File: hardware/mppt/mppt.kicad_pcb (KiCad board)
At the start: 4 copper layers, 160 x 160 mm, 355 parts, among them IC1301 INA229AIDGSR, IC1501 LMR38010SDDAR, IC1502 TPS2121, IC801 INA229AIDGSR, IC901 SN74LVC08APWR, IC902 SN74LVC1G04DBVR, IC903 SN74HCS367PWR, IC904 SN74LVC2G32DCUR, J1401 Conn_01x04, J1402 Conn_01x02, J1403 Conn_02x04_Odd_Even, J1404 Conn_01x10, J1405 USB_C_Plug_USB2.0, J1501 Conn_01x02, J1502 CT3151, J1503 CT3151, J1504 CT3151, J301 Conn_01x01, J302 Conn_01x01, J303 CT3151, J304 CT3151, J305 CT3151, J306 CT3151, J307 Conn_01x01, J308 Conn_01x01, J401 Conn_01x02, J402 Conn_01x03, J403 Conn_01x03, J404 Conn_01x03, Q1001 Q_NMOS_GDS, Q1101 Q_NMOS_SGD, Q1102 Q_NMOS_SGD, Q1201 Q_NMOS_SGD, Q1202 Q_NMOS_SGD, Q401 Q_NMOS_GDS, Q501 EPC2059, Q502 EPC2059, Q601 Q_NMOS_GDS, Q701 Q_NMOS_GDS, SW201 SW_SPST, U1001 ADUM4221-1ARIZ, U1101 TPSI3050, U1201 TPSI3050, U1401 ISO1044BD, U1402 USBLC6-2SC6, U1501 AP63205WU, U1502 TLV75733PDBV, U201 STM32F446RETx, U401 MCP9700Ax-ELT, Y201 16MHz, Y202 32kHz

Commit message: PCB variant for power regulation breakout.
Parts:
- removed C1001, C1003, C1004, C204: 10u, Capacitor_SMD:C_1206_3216Metric_Pad1.33x1.80mm_HandSolder
- removed C1002, C1005, C1006, C1102, C1202, C1301, C1302, C1401, C1402, C203, C205, C208, C209, C211, C212, C213, C801, C802, C901, C902, C903, C904: 100n, Capacitor_SMD:C_0402_1005Metric_Pad0.74x0.62mm_HandSolder
- removed C1101, C1103, C1104, C1201, C1203, C1204, C214, C401, C402: 1u, Capacitor_SMD:C_0603_1608Metric_Pad1.08x0.95mm_HandSolder
- removed C1516, C1517: 22u, Capacitor_SMD:C_1210_3225Metric_Pad1.33x2.70mm_HandSolder
- removed C201, C206: 10p, Capacitor_SMD:C_0402_1005Metric_Pad0.74x0.62mm_HandSolder
- removed C202, C207: 15p, Capacitor_SMD:C_0402_1005Metric_Pad0.74x0.62mm_HandSolder
- removed C210: 4.7u, Capacitor_SMD:C_0805_2012Metric_Pad1.18x1.45mm_HandSolder
- removed C501, C505: 100n, Capacitor_SMD:C_1206_3216Metric_Pad1.33x1.80mm_HandSolder
- removed C502, C506: 1u, Capacitor_SMD:C_2220_5750Metric_Pad1.97x5.40mm_HandSolder
- removed C503, C507: 2.2u, Capacitor_SMD:C_2220_5750Metric_Pad1.97x5.40mm_HandSolder
- removed C504, C508, C509: 18u, Capacitor_THT:C_Radial_D10.0mm_H16.0mm_P5.00mm
- removed D1001, D1003, D1004, D1101, D1201, D401, D601, D701: Schottky, Diode_SMD:D_SOD-123F
- removed D1002, D1005: Zener, Diode_SMD:D_SOD-123F
- removed D1507, D201, D202, D203: RED, LED_SMD:LED_0805_2012Metric_Pad1.15x1.40mm_HandSolder
- removed D501, D503: 150, Diode_SMD:D_SMA_Handsoldering
- removed D502: SMAJ150CA, Diode_SMD:D_SMA_Handsoldering
- removed D602, D702: BLU, LED_SMD:LED_0805_2012Metric_Pad1.15x1.40mm_HandSolder
- removed F501, F502: Fuse, footprints:littelfuse_65600001009
- removed FB201: FerriteBead, Resistor_SMD:R_0603_1608Metric_Pad0.98x0.95mm_HandSolder
- removed H401, H402, H403, H404: MountingHole, MountingHole:MountingHole_2.7mm_M2.5
- removed IC1301, IC801: INA229AIDGSR, footprints:ti_INA229_AIDGSR
- removed IC901: SN74LVC08APWR, footprints:ti_SN74LVC08A_PWR
- removed IC902: SN74LVC1G04DBVR, footprints:ti_SN74LVC1G04_DBVR
- removed IC903: SN74HCS367PWR, footprints:ti_SN74HCS367_PWR
- removed IC904: SN74LVC2G32DCUR, footprints:ti_SN74LVC2G32_DCUR
- removed J1401: Conn_01x04, Connector_Molex:Molex_Micro-Fit_3.0_43650-0415_1x04_P3.00mm_Vertical
- removed J1402: Conn_01x02, Connector_PinHeader_2.54mm:PinHeader_1x02_P2.54mm_Vertical
- removed J1403: Conn_02x04_Odd_Even, Connector_PinHeader_2.54mm:PinHeader_2x04_P2.54mm_Vertical
- removed J1404: Conn_01x10, Connector_PinSocket_2.54mm:PinSocket_1x10_P2.54mm_Vertical
- removed J1405: USB_C_Plug_USB2.0, Connector_USB:USB_C_Receptacle_GCT_USB4105-xx-A_16P_TopMnt_Horizontal
- removed J301, J302, J307, J308: Conn_01x01, footprints:ke_7771_SEMS
- removed J303, J304, J305, J306: CT3151, footprints:caltest_ct3151
- removed J401: Conn_01x02, Connector_Molex:Molex_Micro-Fit_3.0_43650-0215_1x02_P3.00mm_Vertical
- removed J402, J403, J404: Conn_01x03, Connector_Molex:Molex_Micro-Fit_3.0_43650-0315_1x03_P3.00mm_Vertical
- removed JP201: Jumper_3_Bridged12, Connector_PinSocket_2.54mm:PinSocket_1x03_P2.54mm_Vertical
- removed L1503: 10u, Inductor_SMD:L_Bourns_SRN6045TA
- removed L501: 471u, footprints:ferroxcube_PQ32_30_3C97_wire
- removed LB501: CPV-PQ32/30-1S-12P-Z, footprints:ferroxcube_CPV-PQ32_30-1S-12P-Z
- removed NT1001, NT1301, NT601, NT701, NT801: NetTie_2, NetTie:NetTie-2_SMD_Pad0.5mm
- removed NT501: NetTie_3_Tee, NetTie:NetTie-3_SMD_Pad2.0mm
- removed PS1501: CRE1S0505MEC, footprints:murata_CRE1_S0505MEC
- removed Q1001, Q401, Q601, Q701: Q_NMOS_GDS, Package_TO_SOT_SMD:SOT-223-3_TabPin2
- removed Q1101, Q1102, Q1201, Q1202: Q_NMOS_SGD, Package_SO:PowerPAK_SO-8_Single
- removed Q501, Q502: EPC2059, footprints:epc_EPC2059
- removed R1001, R204, R901, R902, R903, R904, R905, R906, R907: 10k, Resistor_SMD:R_0603_1608Metric_Pad0.98x0.95mm_HandSolder
- removed R1002, R1003, R1004, R1005, R203: 0, Resistor_SMD:R_1210_3225Metric_Pad1.30x2.65mm_HandSolder
- removed R1006: 1.5, Resistor_SMD:R_1210_3225Metric_Pad1.30x2.65mm_HandSolder
- removed R1101, R1201: 7.32k, Resistor_SMD:R_0603_1608Metric_Pad0.98x0.95mm_HandSolder
- removed R1102, R1103, R1202, R1203, R601, R602, R701, R702: 15, Resistor_SMD:R_1210_3225Metric_Pad1.30x2.65mm_HandSolder
- removed R1301, R801: 86.6k, Resistor_SMD:R_0603_1608Metric_Pad0.98x0.95mm_HandSolder
- removed R1302, R1402, R1403, R1404, R802: 100k, Resistor_SMD:R_0603_1608Metric_Pad0.98x0.95mm_HandSolder
- removed R1303, R1305, R803, R805: 15, Resistor_SMD:R_0603_1608Metric_Pad0.98x0.95mm_HandSolder
- removed R1304, R804: 4m, Resistor_SMD:R_Shunt_Vishay_WSKW0612
- removed R1401: 120, Resistor_SMD:R_0603_1608Metric_Pad0.98x0.95mm_HandSolder
- removed R1405, R1406: 5.1k, Resistor_SMD:R_0603_1608Metric_Pad0.98x0.95mm_HandSolder
- removed R1520, R201, R202, R205, R401, R402: 3.3k, Resistor_SMD:R_0603_1608Metric_Pad0.98x0.95mm_HandSolder
- removed R403: 205, Resistor_SMD:R_0603_1608Metric_Pad0.98x0.95mm_HandSolder
- removed R603, R703: 10k, Resistor_SMD:R_2512_6332Metric_Pad1.40x3.35mm_HandSolder
- removed the REF** at (138.0, 195.1)
- removed SW201: SW_SPST, Button_Switch_THT:SW_PUSH_6mm
- removed TP1001, TP1002, TP1003, TP1004, TP1005, TP1006, TP1007, TP1101, TP1102, TP1103, TP1104, TP1105, TP1201, TP1202, TP1203, TP1204, TP1205, TP1301, TP1302, TP1303, TP1304, TP1305, TP1306, TP1307, TP1405, TP1406, TP1407, TP1408, TP1409, TP1410, TP1411, TP1412, TP1413, TP1414, TP1415, TP1416, TP1417, TP1418, TP1419, TP1420, TP1421, TP203, TP204, TP205, TP206, TP207, TP208, TP209, TP210, TP404, TP405, TP406, TP407, TP408, TP409, TP601, TP602, TP603, TP604, TP701, TP702, TP703, TP704, TP802, TP803, TP804, TP805, TP806, TP807, TP808, TP901, TP902, TP903, TP904, TP905, TP906: TestPoint_Small, TestPoint:TestPoint_Pad_D1.0mm
- removed TP1308, TP1309, TP503, TP504, TP809, TP810: TestPoint_2Pole, TestPoint:TestPoint_2Pads_Pitch2.54mm_Drill0.8mm
- removed TP1401, TP1402, TP1403, TP1404, TP201, TP202, TP301, TP302, TP303, TP401, TP402, TP403, TP501, TP502, TP505, TP506, TP507: TestPoint, TestPoint:TestPoint_Keystone_5000-5004_Miniature
- removed U1001: ADUM4221-1ARIZ, footprints:ad_ADUM4221_1ARIZ
- removed U1101, U1201: TPSI3050, footprints:ti_TPS3050_DWZ
- removed U1401: ISO1044BD, Package_SO:SOIC-8_3.9x4.9mm_P1.27mm
- removed U1402: USBLC6-2SC6, Package_TO_SOT_SMD:SOT-23-6
- removed U201: STM32F446RETx, Package_QFP:LQFP-64_10x10mm_P0.5mm
- removed U401: MCP9700Ax-ELT, Package_TO_SOT_SMD:SOT-353_SC-70-5
- removed VR1001: PV36W104C01B00, footprints:bourns_PV36W201C01B00
- removed Y201: 16MHz, Crystal:Crystal_SMD_Abracon_ABM8G-4Pin_3.2x2.5mm
- removed Y202: 32kHz, Crystal:Crystal_SMD_Abracon_ABS25-4Pin_8.0x3.8mm
- C1501, C1503, C1507, NT1501, REF** (x2): moved to B.Cu
- C1502, C1505, C1506, C1509, C1510, IC1501, L1501, L1502, R1502, R1513, R1514, R1516, U1501, U1502: moved to F.Cu
- C1511: value 22u -> 1u; footprint Capacitor_SMD:C_1210_3225Metric_Pad1.33x2.70mm_HandSolder -> Capacitor_SMD:C_0603_1608Metric_Pad1.08x0.95mm_HandSolder
- C1512: value 1u -> 10u; footprint Capacitor_SMD:C_0603_1608Metric_Pad1.08x0.95mm_HandSolder -> Capacitor_SMD:C_1206_3216Metric_Pad1.33x1.80mm_HandSolder; moved to B.Cu
- C1513: value 10u -> 100n; footprint Capacitor_SMD:C_1206_3216Metric_Pad1.33x1.80mm_HandSolder -> Capacitor_SMD:C_0402_1005Metric_Pad0.74x0.62mm_HandSolder; moved to B.Cu
- C1514: value 100n -> 22u; footprint Capacitor_SMD:C_0402_1005Metric_Pad0.74x0.62mm_HandSolder -> Capacitor_SMD:C_1210_3225Metric_Pad1.33x2.70mm_HandSolder
- C1515: value 4.7u -> 22u; footprint Capacitor_SMD:C_0805_2012Metric_Pad1.18x1.45mm_HandSolder -> Capacitor_SMD:C_1210_3225Metric_Pad1.33x2.70mm_HandSolder
- D1501: footprint Diode_SMD:D_SMA_Handsoldering -> Diode_SMD:D_SMA
- D1502: footprint Diode_SMD:D_SMA_Handsoldering -> Diode_SMD:D_SMA; moved to B.Cu
- H101, H102, H103, H104: footprint MountingHole:MountingHole_3.2mm_M3 -> MountingHole:MountingHole_2.7mm_M2.5_DIN965_Pad_TopBottom
- REF**: value Symbol_HighVoltage_Triangle_6x6mm_Copper -> Symbol_HighVoltage_NoTriangle_2x5mm_Copper; footprint Symbol:Symbol_HighVoltage_Triangle_6x6mm_Copper -> Symbol:Symbol_HighVoltage_NoTriangle_2x5mm_Copper
- moved J1504 285.0 mm to (54.0, 82.8), turned to 0 degrees
- moved TP1508 269.3 mm to (48.5, 55.0)
- moved J1503 266.0 mm to (70.0, 82.8), turned to 0 degrees
- moved TP1507 264.6 mm to (48.5, 63.0), turned to 90 degrees
- moved TP1506 259.3 mm to (48.5, 71.0)
- moved J1502 251.3 mm to (86.0, 82.8), turned to 0 degrees
- moved TP1504 246.1 mm to (64.0, 57.7)
- moved TP1505 243.6 mm to (64.2, 69.2)
- moved C1511 242.8 mm to (57.0, 58.4), turned to 0 degrees
- moved D1505 234.4 mm to (48.5, 59.0)
- moved R1518 234.4 mm to (48.5, 59.0)
- moved C1515 232.1 mm to (57.5, 65.1), turned to 0 degrees
- moved D1506 226.5 mm to (48.5, 67.0), turned to 90 degrees
- moved R1519 226.5 mm to (48.5, 67.0), turned to 90 degrees
- moved TP1503 225.0 mm to (79.2, 71.4)
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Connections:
- C1512 pad 1: +5V -> +3V3
- C1513 pad 1: +3V3 -> Net-(U1501-BST)
- C1513 pad 2: GND -> Net-(U1501-SW)
- C1514 pad 1: Net-(U1501-BST) -> +5V
- C1514 pad 2: Net-(U1501-SW) -> GND
- C1515 pad 1: +5VL -> +5V
- C1515 pad 2: GND1 -> GND
- IC1501 pad 5: /power regulation/BUCK_PG -> /power regulation/BUCK_FB
- IC1501 pad 6: /power regulation/BUCK_FB -> /power regulation/BUCK_PG
- R1513 pad 2: /power regulation/BUCK_FB -> /power regulation/BUCK_PG
- R1515 pad 2: /power regulation/BUCK_PG -> /power regulation/BUCK_FB
- R1516 pad 1: /power regulation/BUCK_PG -> /power regulation/BUCK_FB
- TP1506 pad 1: +5V -> +12V
- TP1507 pad 1: +5VL -> +5V
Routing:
- net +12V: track 0.00 -> 37.2 mm, vias 0 -> 8
- net +12C: track 0.00 -> 32.1 mm, vias 0 -> 8
- net Net-(JP1501-A): track 0.00 -> 20.3 mm, vias 0 -> 1
- net GND: track 0.00 -> 20.2 mm, vias 0 -> 22
- net /VI-: track 0.00 -> 17.5 mm, vias 0 -> 12
- net +5V: track 0.00 -> 15.1 mm, vias 0 -> 1
- net /VI+: track 1.84 -> 14.0 mm, vias 0 -> 12
- net /power regulation/OV2: track 0.00 -> 8.85 mm, vias 0 -> 1
- net /power regulation/OV1: track 0.00 -> 8.85 mm, vias 0 -> 1
- net /power regulation/PR1: track 0.00 -> 8.07 mm, vias 0 -> 1
- net /power regulation/CP2: track 0.00 -> 7.93 mm, vias 0 -> 1
- net +12L: track 0.00 -> 5.62 mm, vias 0 -> 6
- net +3V3: track 0.00 -> 5.55 mm, vias 0 -> 1
- net /power regulation/BUCK_FB: track 1.85 -> 5.15 mm, vias 0 -> 1
- net Net-(IC1501-EN): track 8.54 -> 5.44 mm, vias 0 -> 1
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- added copper zone on F.Cu, net +12C
- added copper zone on F.Cu, net +12L
- added copper zone on F.Cu, net +12V
- added copper zone on F.Cu, net +3V3
- added copper zone on F.Cu, net +5V
- added copper zone on F.Cu, net /VI+
- added copper zone on B.Cu, net /VI-
- added copper zone on F.Cu, net /VI-
- added copper zone on In1.Cu, net /VI-
- added copper zone on In2.Cu, net /VI-
- added copper zone on B.Cu, net GND
- added copper zone on In1.Cu, net GND
- added copper zone on In2.Cu, net GND
- added copper zone on F.Cu, net Net-(IC1501-SW)
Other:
- board size 160 x 160 mm -> 50 x 50 mm
- board text added: "12C"
- board text added: "12L"
- board text added: "12V"
- board text added: "3V3"
- board text added: "5V"
- board text added: "CARPWR"
- board text added: "GND"
- board text added: "Mighty MPPT Power Regulation Breakout v0.1.0rc Matthew Yu & Jacob Pustilnik"
- board text added: "VI+"
- board text added: "VI-"
- board text removed: "80-150V"
- board text removed: "BANANA FOR SCALE"
- board text removed: "Mighty MPPT Power Converter Breakout v0.1.0rc Matthew Yu & Jacob Pustilnik"

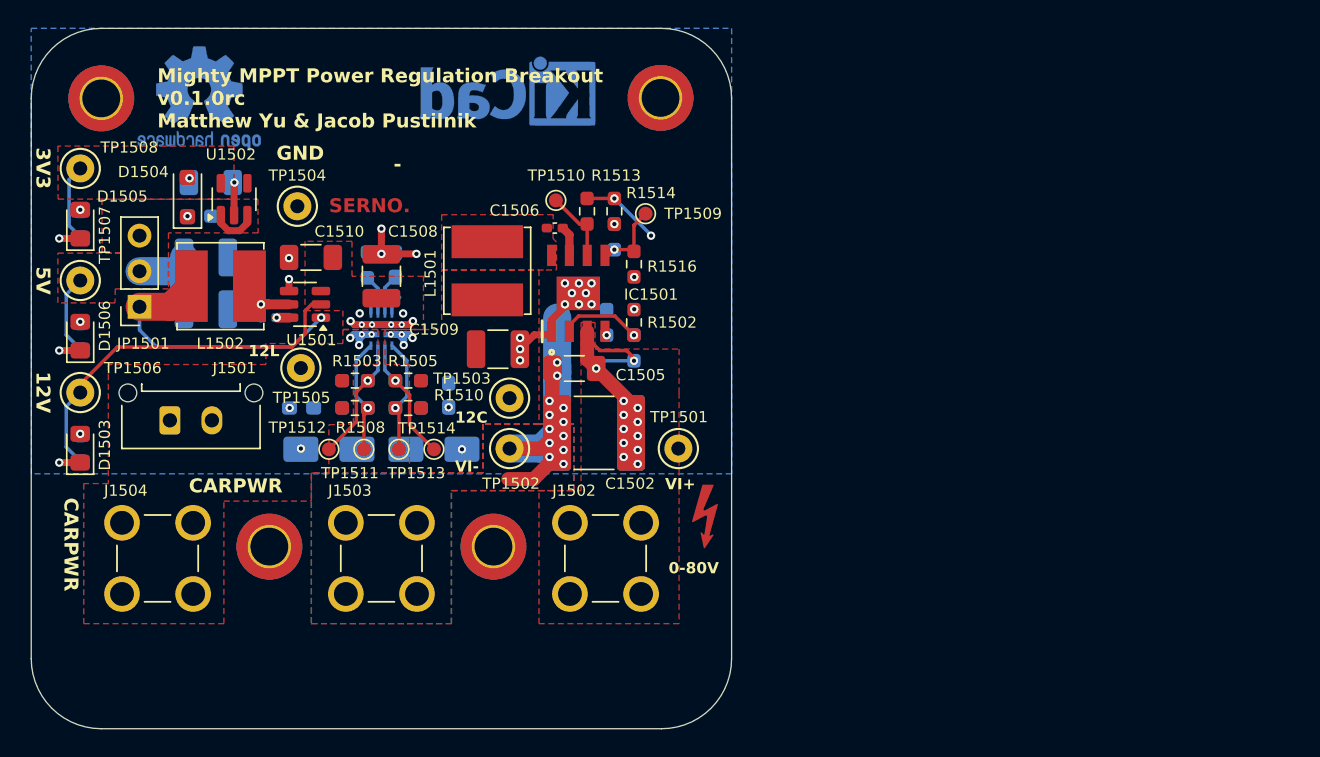
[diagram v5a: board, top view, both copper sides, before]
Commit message: complete layout, drc, signaling optimizations and added dnp testpoints
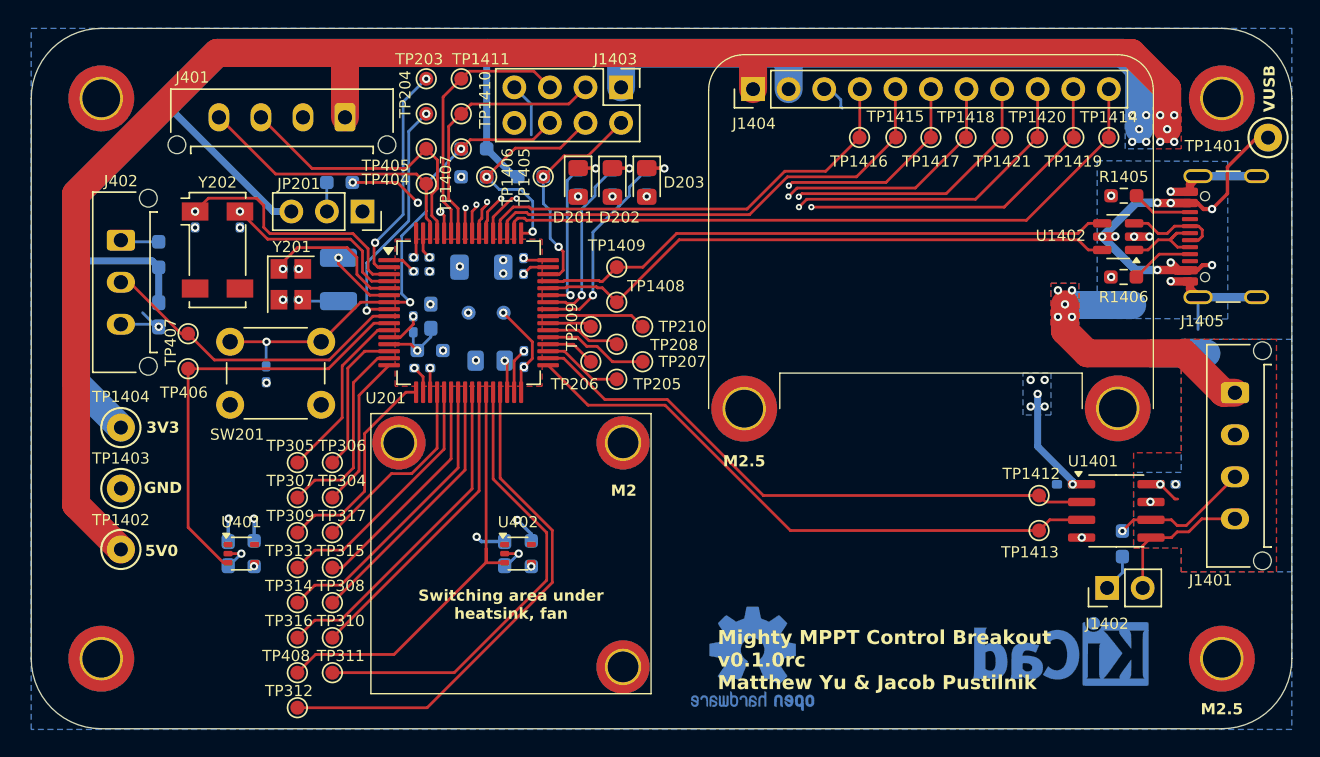
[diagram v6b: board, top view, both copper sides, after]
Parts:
- removed C1501, C1504, C1507, C1511: 1u, Capacitor_SMD:C_0603_1608Metric_Pad1.08x0.95mm_HandSolder
- removed C1502, C1503: 2.2u, Capacitor_SMD:C_2220_5750Metric_Pad1.97x5.40mm_HandSolder
- removed C1505: 100n, Capacitor_SMD:C_1206_3216Metric_Pad1.33x1.80mm_HandSolder
- removed C1506, C1513: 100n, Capacitor_SMD:C_0402_1005Metric_Pad0.74x0.62mm_HandSolder
- removed C1508, C1509, C1514, C1515: 22u, Capacitor_SMD:C_1210_3225Metric_Pad1.33x2.70mm_HandSolder
- removed C1510, C1512: 10u, Capacitor_SMD:C_1206_3216Metric_Pad1.33x1.80mm_HandSolder
- removed D1501, D1502: SMAJ15CA, Diode_SMD:D_SMA
- removed D1503, D1505, D1506: RED, LED_SMD:LED_0805_2012Metric_Pad1.15x1.40mm_HandSolder
- removed D1504: Schottky, Diode_SMD:D_SOD-123F
- removed IC1501: LMR38010SDDAR, footprints:ti_LMR38010_SDDAR
- removed IC1502: TPS2121, footprints:ti_TPS2121_RUXR
- removed J1501: Conn_01x02, Connector_Molex:Molex_Micro-Fit_3.0_43650-0215_1x02_P3.00mm_Vertical
- removed J1502, J1503, J1504: CT3151, footprints:caltest_ct3151
- removed JP1501: Jumper_3_Bridged12, Connector_PinSocket_2.54mm:PinSocket_1x03_P2.54mm_Vertical
- removed L1501: 68u, Inductor_SMD:L_Bourns_SRN6045TA
- removed L1502: 4.7u, Inductor_SMD:L_Bourns_SRN6045TA
- removed NT1501: NetTie_2, NetTie:NetTie-2_SMD_Pad2.0mm
- removed R1501, R1503, R1505, R1508, R1510, R1513, R1514: 100k, Resistor_SMD:R_0603_1608Metric_Pad0.98x0.95mm_HandSolder
- removed R1502, R1515, R1516, R1517: 10k, Resistor_SMD:R_0603_1608Metric_Pad0.98x0.95mm_HandSolder
- removed R1504, R1506: 7.68k, Resistor_SMD:R_0603_1608Metric_Pad0.98x0.95mm_HandSolder
- removed R1507, R1512: 64.9k, Resistor_SMD:R_0603_1608Metric_Pad0.98x0.95mm_HandSolder
- removed R1509: 17.4k, Resistor_SMD:R_0603_1608Metric_Pad0.98x0.95mm_HandSolder
- removed R1511: 14k, Resistor_SMD:R_0603_1608Metric_Pad0.98x0.95mm_HandSolder
- removed R1518, R1519: 3.3k, Resistor_SMD:R_0603_1608Metric_Pad0.98x0.95mm_HandSolder
- removed the REF** at (93.3, 80.0)
- removed TP1501, TP1502, TP1503, TP1504, TP1505, TP1506, TP1507, TP1508: TestPoint, TestPoint:TestPoint_Keystone_5000-5004_Miniature
- removed TP1509, TP1510, TP1511, TP1512, TP1513, TP1514: TestPoint_Small, TestPoint:TestPoint_Pad_D1.0mm
- removed U1501: AP63205WU, Package_TO_SOT_SMD:TSOT-23-6
- removed U1502: TLV75733PDBV, Package_TO_SOT_SMD:SOT-23-5
- added C1401: 100n, Capacitor_SMD:C_0402_1005Metric_Pad0.74x0.62mm_HandSolder, B.Cu at (118.8, 77.5)
- added C1402: 100n, Capacitor_SMD:C_0402_1005Metric_Pad0.74x0.62mm_HandSolder, B.Cu at (126.1, 77.5)
- added C201: 10p, Capacitor_SMD:C_0402_1005Metric_Pad0.74x0.62mm_HandSolder, B.Cu at (63.5, 62.2)
- added C202: 15p, Capacitor_SMD:C_0402_1005Metric_Pad0.74x0.62mm_HandSolder, B.Cu at (56.7, 58.6)
- added C203: 100n, Capacitor_SMD:C_0402_1005Metric_Pad0.74x0.62mm_HandSolder, B.Cu at (61.8, 69.7)
- added C204: 10u, Capacitor_SMD:C_1206_3216Metric_Pad1.33x1.80mm_HandSolder, B.Cu at (77.1, 62.0)
- added C205: 100n, Capacitor_SMD:C_0402_1005Metric_Pad0.74x0.62mm_HandSolder, B.Cu at (72.9, 61.4)
- added C206: 10p, Capacitor_SMD:C_0402_1005Metric_Pad0.74x0.62mm_HandSolder, B.Cu at (63.5, 64.4)
- added C207: 15p, Capacitor_SMD:C_0402_1005Metric_Pad0.74x0.62mm_HandSolder, B.Cu at (59.9, 58.6)
- added C208: 100n, Capacitor_SMD:C_0402_1005Metric_Pad0.74x0.62mm_HandSolder, B.Cu at (80.2, 62.0)
- added C209: 100n, Capacitor_SMD:C_0402_1005Metric_Pad0.74x0.62mm_HandSolder, B.Cu at (72.9, 62.4)
- added C210: 4.7u, Capacitor_SMD:C_0805_2012Metric_Pad1.18x1.45mm_HandSolder, B.Cu at (77.8, 68.7)
- added C211: 100n, Capacitor_SMD:C_0402_1005Metric_Pad0.74x0.62mm_HandSolder, B.Cu at (80.2, 68.6)
- added C212: 100n, Capacitor_SMD:C_0402_1005Metric_Pad0.74x0.62mm_HandSolder, B.Cu at (72.9, 69.2)
- added C213: 100n, Capacitor_SMD:C_0402_1005Metric_Pad0.74x0.62mm_HandSolder, B.Cu at (72.3, 66.1)
- added C214: 1u, Capacitor_SMD:C_0603_1608Metric_Pad1.08x0.95mm_HandSolder, B.Cu at (73.5, 65.5)
- added C401: 1u, Capacitor_SMD:C_0603_1608Metric_Pad1.08x0.95mm_HandSolder, B.Cu at (59.1, 82.5)
- added C402: 1u, Capacitor_SMD:C_0603_1608Metric_Pad1.08x0.95mm_HandSolder, B.Cu at (78.8, 82.5)
- added C403: 1u, Capacitor_SMD:C_0603_1608Metric_Pad1.08x0.95mm_HandSolder, B.Cu at (54.1, 65.5)
- added D201: RED, LED_SMD:LED_0805_2012Metric_Pad1.15x1.40mm_HandSolder, F.Cu at (84.0, 56.0)
- added D202: RED, LED_SMD:LED_0805_2012Metric_Pad1.15x1.40mm_HandSolder, F.Cu at (86.5, 56.0)
- added D203: RED, LED_SMD:LED_0805_2012Metric_Pad1.15x1.40mm_HandSolder, F.Cu at (88.9, 56.0)
- added FB201: FerriteBead, Resistor_SMD:R_0603_1608Metric_Pad0.98x0.95mm_HandSolder, B.Cu at (73.5, 68.0)
- added H1401: MountingHole, MountingHole:MountingHole_2.7mm_M2.5_DIN965_Pad_TopBottom, F.Cu at (95.9, 72.2)
- added H1402: MountingHole, MountingHole:MountingHole_2.7mm_M2.5_DIN965_Pad_TopBottom, F.Cu at (122.6, 72.1)
- added H401: MountingHole, MountingHole:MountingHole_2.2mm_M2_DIN965_Pad_TopBottom, F.Cu at (87.2, 74.6)
- added H402: MountingHole, MountingHole:MountingHole_2.2mm_M2_DIN965_Pad_TopBottom, F.Cu at (71.2, 74.6)
- added H403: MountingHole, MountingHole:MountingHole_2.2mm_M2_DIN965_Pad_TopBottom, F.Cu at (87.2, 90.6)
- added J1401: Conn_01x04, Connector_Molex:Molex_Micro-Fit_3.0_43650-0415_1x04_P3.00mm_Vertical, F.Cu at (130.9, 71.0)
- added J1402: Conn_01x02, Connector_PinHeader_2.54mm:PinHeader_1x02_P2.54mm_Vertical, F.Cu at (121.8, 85.0)
- added J1403: Conn_02x04_Odd_Even, Connector_PinHeader_2.54mm:PinHeader_2x04_P2.54mm_Vertical, F.Cu at (87.1, 49.2)
- added J1404: Conn_01x11, Connector_PinHeader_2.54mm:PinHeader_1x11_P2.54mm_Vertical, F.Cu at (96.5, 49.3)
- added J1405: USB_C_Plug_USB2.0, Connector_USB:USB_C_Receptacle_GCT_USB4105-xx-A_16P_TopMnt_Horizontal, F.Cu at (131.4, 59.9)
- added J401: Conn_01x04, Connector_Molex:Molex_Micro-Fit_3.0_43650-0415_1x04_P3.00mm_Vertical, F.Cu at (67.4, 51.4)
- added J402: Conn_01x03, Connector_Molex:Molex_Micro-Fit_3.0_43650-0315_1x03_P3.00mm_Vertical, F.Cu at (51.4, 60.1)
- added JP201: Jumper_3_Bridged12, Connector_PinSocket_2.54mm:PinSocket_1x03_P2.54mm_Vertical, F.Cu at (68.7, 58.1)
- added NT1401: NetTie_2, NetTie:NetTie-2_SMD_Pad2.0mm, B.Cu at (126.9, 68.2)
- added NT1402: NetTie_2, NetTie:NetTie-2_SMD_Pad2.0mm, B.Cu at (121.6, 64.8)
- added R1401: 120, Resistor_SMD:R_0603_1608Metric_Pad0.98x0.95mm_HandSolder, B.Cu at (122.9, 81.8)
- added R1402: 100k, Resistor_SMD:R_0603_1608Metric_Pad0.98x0.95mm_HandSolder, B.Cu at (76.6, 53.6)
- added R1403: 100k, Resistor_SMD:R_0603_1608Metric_Pad0.98x0.95mm_HandSolder, B.Cu at (80.7, 55.6)
- added R1404: 100k, Resistor_SMD:R_0603_1608Metric_Pad0.98x0.95mm_HandSolder, B.Cu at (76.6, 55.6)
- added R1405: 5.1k, Resistor_SMD:R_0603_1608Metric_Pad0.98x0.95mm_HandSolder, F.Cu at (123.0, 57.0)
- added R1406: 5.1k, Resistor_SMD:R_0603_1608Metric_Pad0.98x0.95mm_HandSolder, F.Cu at (123.0, 62.8)
- added R201: 3.3k, Resistor_SMD:R_0603_1608Metric_Pad0.98x0.95mm_HandSolder, B.Cu at (84.0, 56.0)
- added R202: 3.3k, Resistor_SMD:R_0603_1608Metric_Pad0.98x0.95mm_HandSolder, B.Cu at (86.5, 56.0)
- added R203: 0, Resistor_SMD:R_1210_3225Metric_Pad1.30x2.65mm_HandSolder, B.Cu at (66.9, 62.9)
- added R204: 100k, Resistor_SMD:R_0603_1608Metric_Pad0.98x0.95mm_HandSolder, B.Cu at (67.0, 56.0)
- added R205: 3.3k, Resistor_SMD:R_0603_1608Metric_Pad0.98x0.95mm_HandSolder, B.Cu at (88.9, 56.0)
- added R401: 205, Resistor_SMD:R_0603_1608Metric_Pad0.98x0.95mm_HandSolder, B.Cu at (60.9, 82.5)
- added R402: 205, Resistor_SMD:R_0603_1608Metric_Pad0.98x0.95mm_HandSolder, B.Cu at (80.7, 82.5)
- added R403: 205, Resistor_SMD:R_0603_1608Metric_Pad0.98x0.95mm_HandSolder, B.Cu at (54.1, 61.1)
- added SW201: SW_SPST, Button_Switch_THT:SW_PUSH_6mm, F.Cu at (65.7, 71.9)
- added TP1401: TestPoint, TestPoint:TestPoint_Keystone_5000-5004_Miniature, F.Cu at (133.3, 52.8)
- added TP1402: TestPoint, TestPoint:TestPoint_Keystone_5000-5004_Miniature, F.Cu at (51.4, 82.2)
- added TP1403: TestPoint, TestPoint:TestPoint_Keystone_5000-5004_Miniature, F.Cu at (51.4, 77.8)
- added TP1404: TestPoint, TestPoint:TestPoint_Keystone_5000-5004_Miniature, F.Cu at (51.4, 73.5)
- added TP1405: TestPoint_Small, TestPoint:TestPoint_Pad_D1.0mm, F.Cu at (81.5, 55.6)
- added TP1406: TestPoint_Small, TestPoint:TestPoint_Pad_D1.0mm, F.Cu at (77.5, 55.6)
- added TP1407: TestPoint_Small, TestPoint:TestPoint_Pad_D1.0mm, F.Cu at (75.7, 53.6)
- added TP1408: TestPoint_Small, TestPoint:TestPoint_Pad_D1.0mm, F.Cu at (86.8, 64.5)
- added TP1409: TestPoint_Small, TestPoint:TestPoint_Pad_D1.0mm, F.Cu at (86.8, 62.0)
- added TP1410: TestPoint_Small, TestPoint:TestPoint_Pad_D1.0mm, F.Cu at (75.7, 51.1)
- added TP1411: TestPoint_Small, TestPoint:TestPoint_Pad_D1.0mm, F.Cu at (75.7, 48.6)
- added TP1412: TestPoint_Small, TestPoint:TestPoint_Pad_D1.0mm, F.Cu at (117.0, 78.3)
- added TP1413: TestPoint_Small, TestPoint:TestPoint_Pad_D1.0mm, F.Cu at (117.0, 80.8)
- added TP1414: TestPoint_Small, TestPoint:TestPoint_Pad_D1.0mm, F.Cu at (121.9, 52.8)
- added TP1415: TestPoint_Small, TestPoint:TestPoint_Pad_D1.0mm, F.Cu at (106.7, 52.8)
- added TP1416: TestPoint_Small, TestPoint:TestPoint_Pad_D1.0mm, F.Cu at (104.1, 52.8)
- added TP1417: TestPoint_Small, TestPoint:TestPoint_Pad_D1.0mm, F.Cu at (109.2, 52.8)
- added TP1418: TestPoint_Small, TestPoint:TestPoint_Pad_D1.0mm, F.Cu at (111.7, 52.8)
- added TP1419: TestPoint_Small, TestPoint:TestPoint_Pad_D1.0mm, F.Cu at (119.4, 52.8)
- added TP1420: TestPoint_Small, TestPoint:TestPoint_Pad_D1.0mm, F.Cu at (116.8, 52.8)
- added TP1421: TestPoint_Small, TestPoint:TestPoint_Pad_D1.0mm, F.Cu at (114.3, 52.8)
- added TP201: TestPoint_Small, TestPoint:TestPoint_Pad_D1.0mm, B.Cu at (78.7, 65.3)
- added TP202: TestPoint_Small, TestPoint:TestPoint_Pad_D1.0mm, B.Cu at (76.2, 65.3)
- added TP203: TestPoint_Small, TestPoint:TestPoint_Pad_D1.0mm, F.Cu at (73.2, 48.6)
- added TP204: TestPoint_Small, TestPoint:TestPoint_Pad_D1.0mm, F.Cu at (73.2, 51.1)
- added TP205: TestPoint_Small, TestPoint:TestPoint_Pad_D1.0mm, F.Cu at (86.8, 70.0)
- added TP206: TestPoint_Small, TestPoint:TestPoint_Pad_D1.0mm, F.Cu at (85.0, 68.8)
- added TP207: TestPoint_Small, TestPoint:TestPoint_Pad_D1.0mm, F.Cu at (88.7, 68.8)
- added TP208: TestPoint_Small, TestPoint:TestPoint_Pad_D1.0mm, F.Cu at (86.8, 67.5)
- added TP209: TestPoint_Small, TestPoint:TestPoint_Pad_D1.0mm, F.Cu at (85.0, 66.3)
- added TP210: TestPoint_Small, TestPoint:TestPoint_Pad_D1.0mm, F.Cu at (88.7, 66.3)
- added TP304: TestPoint_Small, TestPoint:TestPoint_Pad_D1.0mm, F.Cu at (66.5, 78.5)
- added TP305: TestPoint_Small, TestPoint:TestPoint_Pad_D1.0mm, F.Cu at (64.0, 76.0)
- added TP306: TestPoint_Small, TestPoint:TestPoint_Pad_D1.0mm, F.Cu at (66.5, 76.0)
- added TP307: TestPoint_Small, TestPoint:TestPoint_Pad_D1.0mm, F.Cu at (64.0, 78.5)
- added TP308: TestPoint_Small, TestPoint:TestPoint_Pad_D1.0mm, F.Cu at (66.5, 86.0)
- added TP309: TestPoint_Small, TestPoint:TestPoint_Pad_D1.0mm, F.Cu at (64.0, 81.0)
- added TP310: TestPoint_Small, TestPoint:TestPoint_Pad_D1.0mm, F.Cu at (66.5, 88.5)
- added TP311: TestPoint_Small, TestPoint:TestPoint_Pad_D1.0mm, F.Cu at (66.5, 91.0)
- added TP312: TestPoint_Small, TestPoint:TestPoint_Pad_D1.0mm, F.Cu at (64.0, 93.5)
- added TP313: TestPoint_Small, TestPoint:TestPoint_Pad_D1.0mm, F.Cu at (64.0, 83.5)
- added TP314: TestPoint_Small, TestPoint:TestPoint_Pad_D1.0mm, F.Cu at (64.0, 86.0)
- added TP315: TestPoint_Small, TestPoint:TestPoint_Pad_D1.0mm, F.Cu at (66.5, 83.5)
- added TP316: TestPoint_Small, TestPoint:TestPoint_Pad_D1.0mm, F.Cu at (64.0, 88.5)
- added TP317: TestPoint_Small, TestPoint:TestPoint_Pad_D1.0mm, F.Cu at (66.5, 81.0)
- added TP404: TestPoint_Small, TestPoint:TestPoint_Pad_D1.0mm, F.Cu at (73.2, 56.1)
- added TP405: TestPoint_Small, TestPoint:TestPoint_Pad_D1.0mm, F.Cu at (73.2, 53.6)
- added TP406: TestPoint_Small, TestPoint:TestPoint_Pad_D1.0mm, F.Cu at (56.2, 69.3)
- added TP407: TestPoint_Small, TestPoint:TestPoint_Pad_D1.0mm, F.Cu at (56.2, 66.8)
- added TP408: TestPoint_Small, TestPoint:TestPoint_Pad_D1.0mm, F.Cu at (64.0, 91.0)
- added U1401: ISO1044BD, Package_SO:SOIC-8_3.9x4.9mm_P1.27mm, F.Cu at (122.5, 79.5)
- added U1402: USBLC6-2SC6, Package_TO_SOT_SMD:SOT-23-6, F.Cu at (122.6, 59.9)
- added U201: STM32F446RETx, Package_QFP:LQFP-64_10x10mm_P0.5mm, F.Cu at (76.2, 65.3)
- added U401: MCP9700Ax-ELT, Package_TO_SOT_SMD:SOT-353_SC-70-5, F.Cu at (60.0, 82.5)
- added U402: MCP9700Ax-ELT, Package_TO_SOT_SMD:SOT-353_SC-70-5, F.Cu at (79.8, 82.5)
- added Y201: 16MHz, Crystal:Crystal_SMD_Abracon_ABM8G-4Pin_3.2x2.5mm, F.Cu at (63.5, 63.3)
- added Y202: 32kHz, Crystal:Crystal_SMD_Abracon_ABS25-4Pin_8.0x3.8mm, F.Cu at (58.3, 60.8)
- moved REF** 56.2 mm to (96.5, 90.0)
- moved REF** 56.2 mm to (118.5, 90.0)
- moved H104 52.6 mm to (130.0, 90.0)
- moved H102 40.1 mm to (130.0, 50.0)
- moved H103 14.4 mm to (50.0, 90.0)
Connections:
- H101 pad 1: (no net) -> unconnected-(H101-Pad1)
- H102 pad 1: (no net) -> unconnected-(H102-Pad1)_2
- H103 pad 1: (no net) -> unconnected-(H103-Pad1)_1
- H104 pad 1: (no net) -> unconnected-(H104-Pad1)_2
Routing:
- net +3V3: track 5.55 -> 276.9 mm, vias 1 -> 24
- net +5V: track 15.1 -> 155.0 mm, vias 1 -> 11
- net /SDC_CS: track 0.00 -> 51.9 mm, vias 0 -> 2
- net /BACKLIGHT_PWM: track 0.00 -> 49.3 mm
- net /DC: track 0.00 -> 48.6 mm, vias 0 -> 2
- net /RESET: track 0.00 -> 45.4 mm, vias 0 -> 2
- net /CAN_RX: track 0.00 -> 43.3 mm
- net /CAN_TX: track 0.00 -> 42.3 mm
- net /USB+: track 0.00 -> 42.2 mm
- net /LCD_CS: track 0.00 -> 42.0 mm, vias 0 -> 2
- net /USB-: track 0.00 -> 41.3 mm
- net /LCD_SPI_COPI: track 0.00 -> 38.6 mm, vias 0 -> 2
- net +12V: track 37.2 -> 0.00 mm, vias 8 -> 0
- net /AL_OUT_EN: track 0.00 -> 37.0 mm
- net /NRST: track 0.00 -> 35.8 mm, vias 0 -> 3
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- added copper zone on B.Cu, net +3V3
- added copper zone on In1.Cu, net +3V3
- added copper zone on In2.Cu, net +3V3
- added copper zone on B.Cu, net +5V
- added copper zone on In1.Cu, net +5V
- added copper zone on B.Cu, net /VUSB
- added copper zone on B.Cu, net GND1
- added copper zone on In1.Cu, net GND1
- added copper zone on In2.Cu, net GND1
- removed copper zone on F.Cu, net +12C
- removed copper zone on F.Cu, net +12L
- removed copper zone on F.Cu, net +12V
- removed copper zone on F.Cu, net /VI+
- removed copper zone on B.Cu, net /VI-
- removed copper zone on F.Cu, net /VI-
- removed copper zone on In1.Cu, net /VI-
- removed copper zone on In2.Cu, net /VI-
- removed copper zone on F.Cu, net Net-(IC1501-SW)
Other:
- board size 50 x 50 mm -> 90 x 50 mm
- board text added: "5V0"
- board text added: "M2"
- board text added: "M2.5"
- board text added: "Mighty MPPT Control Breakout v0.1.0rc Matthew Yu & Jacob Pustilnik"
- board text added: "Swap down to 0603."
- board text added: "Switching area under heatsink, fan"
- board text added: "VUSB"
- board text removed: "-"
- board text removed: "0-80V"
- board text removed: "12C"
- board text removed: "12L"
- board text removed: "12V"
- board text removed: "5V"
- board text removed: "CARPWR"
- board text removed: "Mighty MPPT Power Regulation Breakout v0.1.0rc Matthew Yu & Jacob Pustilnik"
- board text removed: "SERNO."
- board text removed: "VI+"
- board text removed: "VI-"
